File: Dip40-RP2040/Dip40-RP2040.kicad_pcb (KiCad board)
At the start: 2 copper layers, 18.5 x 51.6 mm, 35 parts, among them J2 SKRKAEE020, J3 2.54mm header 01x20, J4 2.54mm header 01x20, J5 Conn_01x03_Male, U1 TPS63002, U3 RP2040, X1 XO 32 12Mhz 3225 seiko

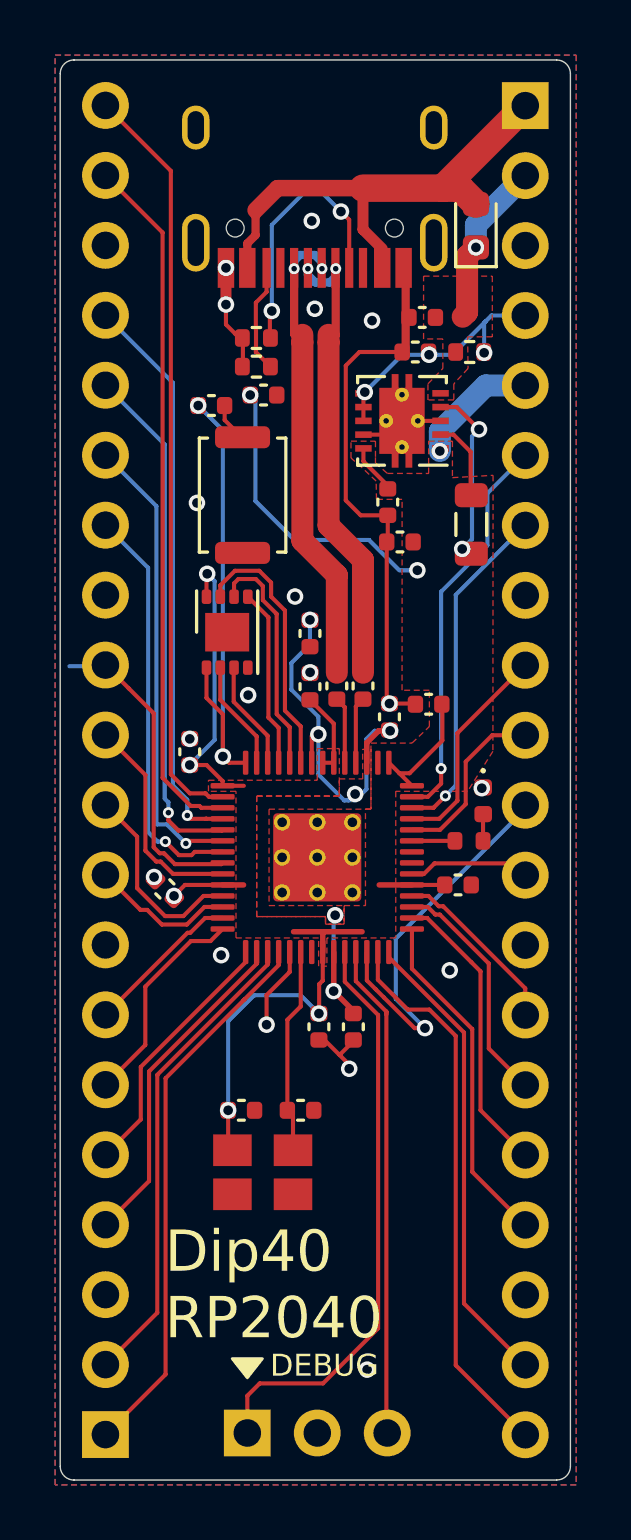
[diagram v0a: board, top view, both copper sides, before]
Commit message: Hopefully implemented ADC_VREF Correctly on dip40 and pico verrsion
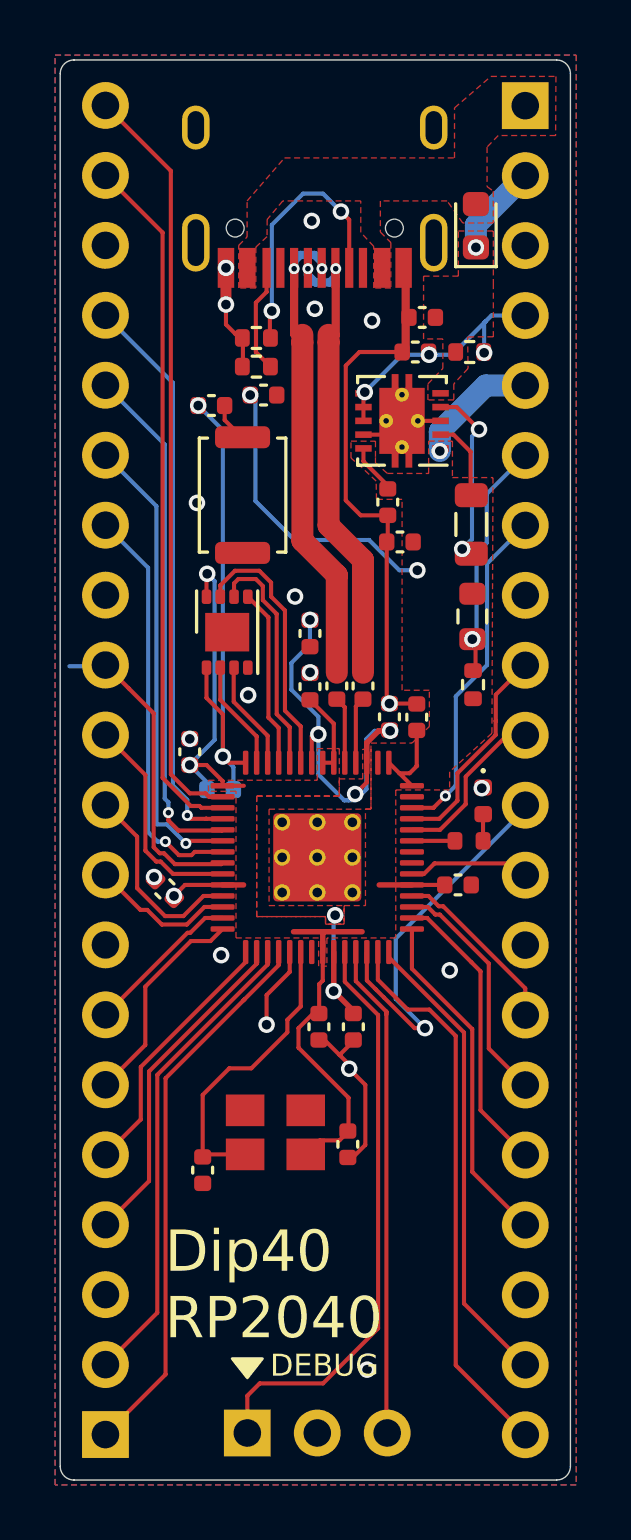
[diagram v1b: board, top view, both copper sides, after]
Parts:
- added R10: 1ohm 0402, Resistor_SMD:R_0402_1005Metric, F.Cu at (109.3, 79.8)
- added R2: DNF, Capacitor_SMD:C_0402_1005Metric, B.Cu at (100.2, 83.6)
- added R9: 100ohm 0603, Resistor_SMD:R_0603_1608Metric, F.Cu at (109.3, 77.3)
- moved C2 4.17 mm to (99.5, 97.4), turned to 90 degrees
- moved C15 4.06 mm to (104.8, 96.4), turned to 270 degrees
- moved X1 1.52 mm to (102.2, 96.0), turned to 180 degrees
- moved C10 0.64 mm to (107.3, 80.9), turned to 90 degrees
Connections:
- FLASH1 pad 9: Net-(FLASH1-Pad9) -> (no net)
- J4 pad 6: /GPIO29_ADC3 -> /ADC_VREF
- U3 pad 21: /XOUT -> (no net)
- U3 pad 35: /GPIO23 -> (no net)
- U3 pad 36: /GPIO24 -> (no net)
- U3 pad 41: /GPIO29_ADC3 -> (no net)
- X1 pad 1: Net-(X1-Pad1) -> (no net)
- e1 pad 3: Net-(e1-Pad3) -> (no net)
- e1 pad 9: Net-(e1-Pad9) -> (no net)
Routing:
- net VBUS: track 24.3 -> 3.35 mm
- net /GPIO29_ADC3: track 14.4 -> 0.00 mm, vias 1 -> 0
- net /ADC_VREF: track 0.00 -> 8.88 mm, vias 0 -> 1
- net GND: track 31.8 -> 35.6 mm
- net /XIN: track 7.48 -> 11.2 mm
- net +3V3: track 54.9 -> 53.2 mm, vias 8 -> 6
- net /QSPI_SS: track 17.5 -> 18.9 mm
- net +1V1: track 20.2 -> 21.5 mm

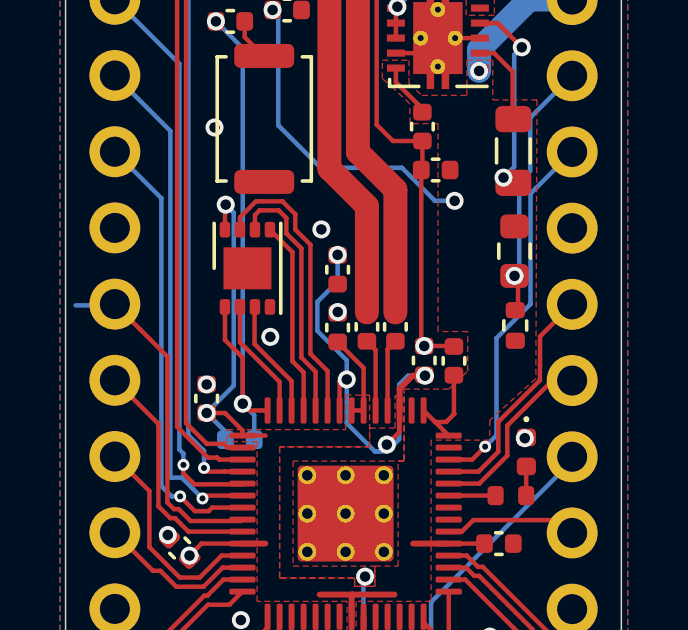
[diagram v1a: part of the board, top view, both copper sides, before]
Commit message: corrected capacitor placement.
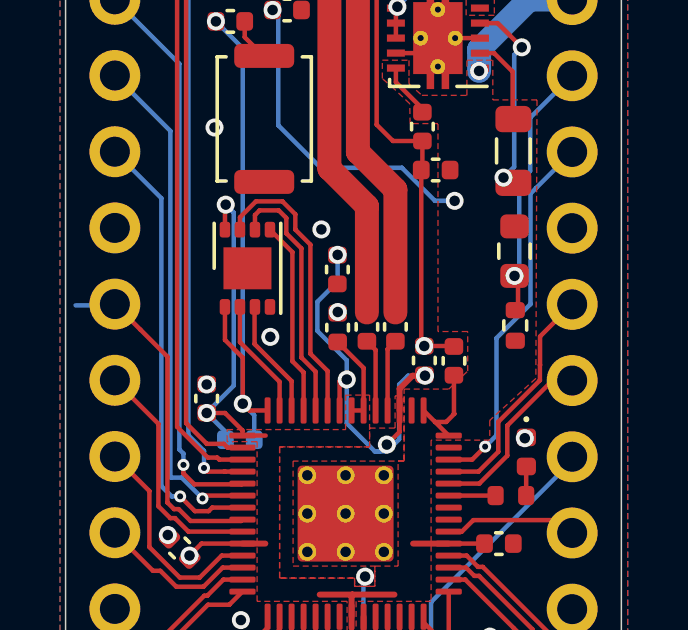
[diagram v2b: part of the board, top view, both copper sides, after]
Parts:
- moved C7 4.19 mm to (103.4, 77.9), turned to 270 degrees
- moved C3 4.18 mm to (106.3, 80.9), turned to 90 degrees
